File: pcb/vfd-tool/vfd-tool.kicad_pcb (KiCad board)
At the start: 4 copper layers, 95 x 50 mm, 170 parts, among them J1 Conn_ARM_SWD_TagConnect_TC203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, J2 USB_C_Receptacle_USB2.0, J3 Micro_SD_Card, J4 Conn_01x10, J5 Raspberry_Pi_2_3, J6 Conn_02x15_Odd_Even, J7 Conn_02x15_Odd_Even, J8 Conn_02x08_Odd_Even, J9 Conn_01x02_Socket, SW1 SW_Push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

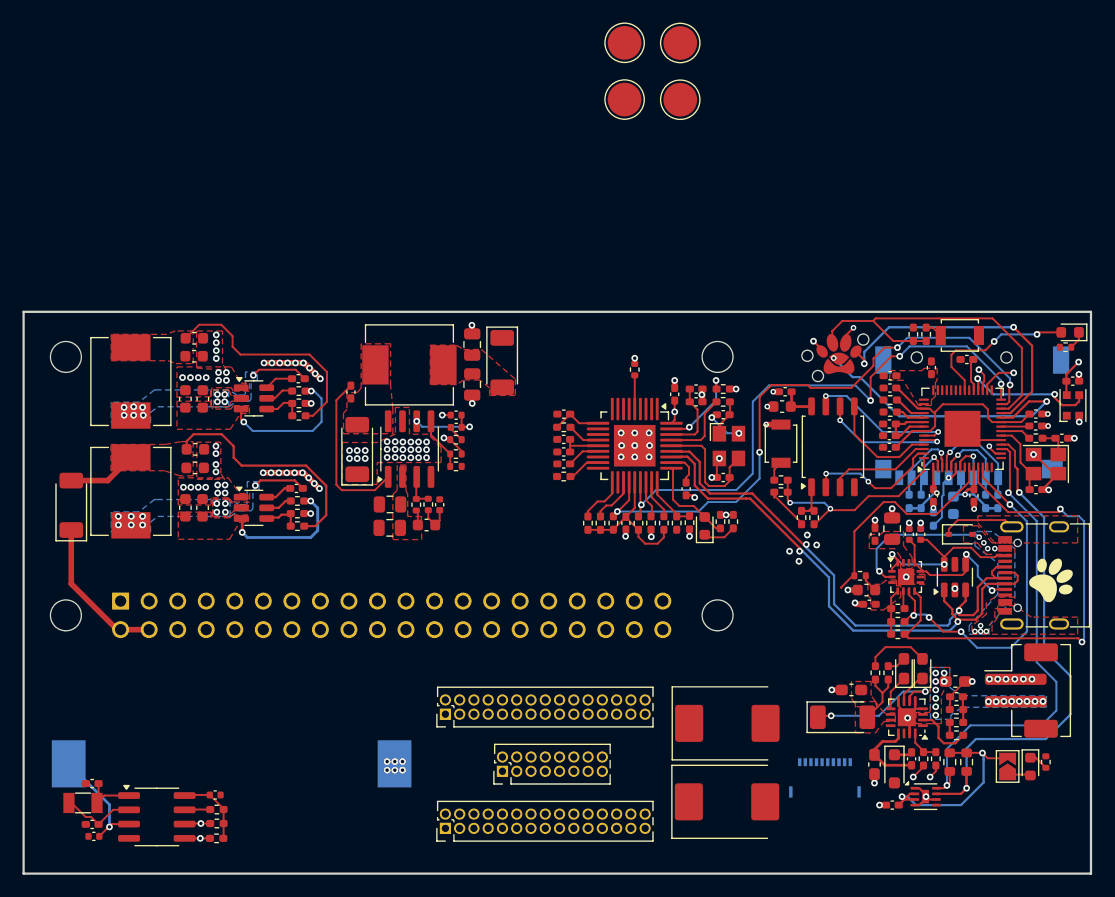
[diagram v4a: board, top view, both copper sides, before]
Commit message: finished interconnect, started on internal power layer
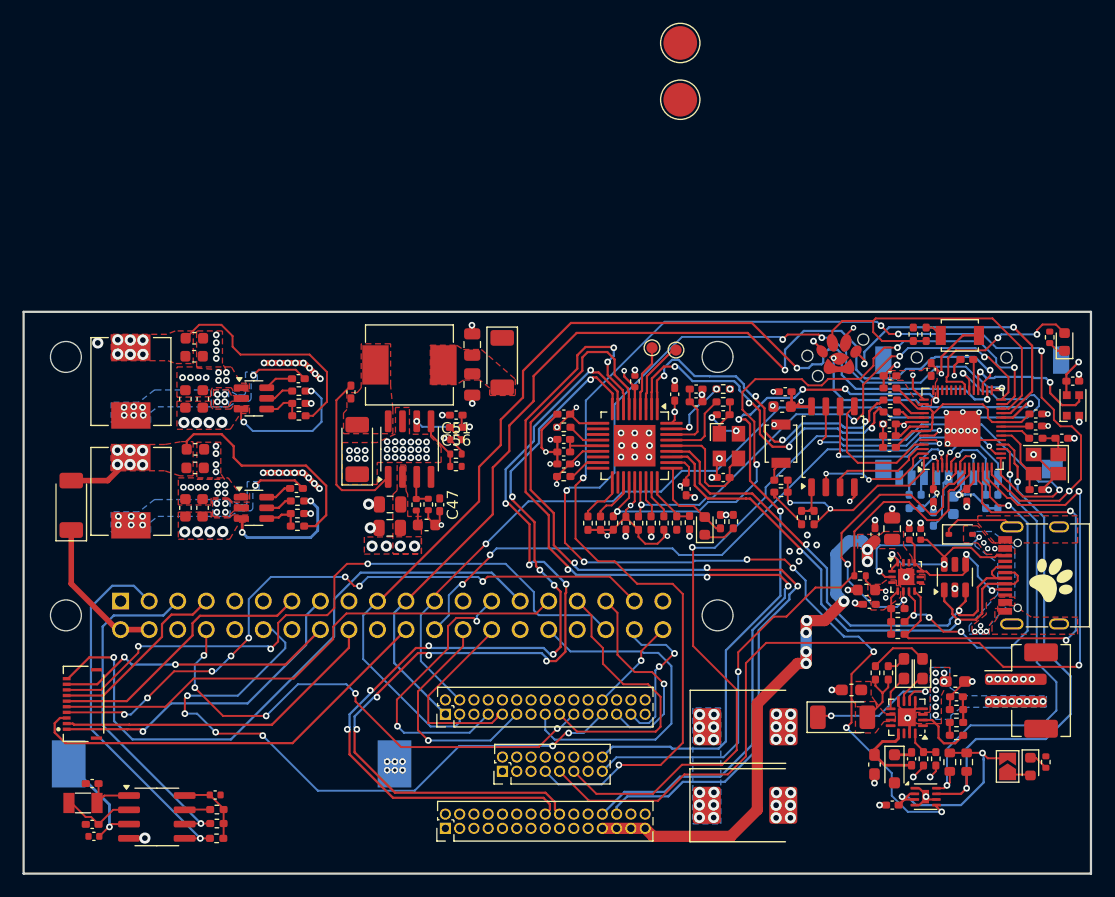
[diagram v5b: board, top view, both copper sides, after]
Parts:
- C47, C51, C56: footprint Capacitor_SMD:C_0402_1005Metric -> Capacitor_SMD:C_0402_1005Metric_Pad0.74x0.62mm_HandSolder
- J4: moved to F.Cu
- TP3, TP4: footprint TestPoint:TestPoint_Pad_D3.0mm -> TestPoint:TestPoint_Pad_D1.0mm
- moved J4 67.7 mm to (145.6, 108.3), turned to 90 degrees
- moved TP4 27.7 mm to (199.8, 76.8)
- moved TP3 22.2 mm to (197.7, 76.6)
- moved R20 1.66 mm to (233.1, 75.7), turned to 90 degrees
- moved D7 1.63 mm to (206.0, 110.3)
- moved D8 1.63 mm to (205.9, 117.3)
- moved C16 1.05 mm to (196.1, 79.6)
- moved D4 0.98 mm to (234.4, 76.1), turned to 90 degrees
- moved C21 0.64 mm to (225.7, 89.7)
- moved C24 0.15 mm to (222.5, 78.5)
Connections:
- J6 pad 11: VBUS -> 5V
- J6 pad 13: GND -> 5V
- J6 pad 15: 3V3 -> GND
- J6 pad 17: 3V3 -> VBUS
- J6 pad 19: 5V -> VBUS
- J6 pad 21: 5V -> VBUS
- J6 pad 26: EXTRA_USB4_D- -> EXTRA_USB3_D-
- J6 pad 7: VBUS -> 3V3
- J6 pad 9: VBUS -> 3V3
- J8 pad 10: GND -> unconnected-(J8-Pin_10-Pad10)
- J8 pad 12: RP2040_GPIO27 -> unconnected-(J8-Pin_12-Pad12)
- J8 pad 14: RP2040_GPIO28 -> unconnected-(J8-Pin_14-Pad14)
- U9 pad 5: GPIO16 -> BATT_INT
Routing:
- net RP2040_GPIO11: track 0.00 -> 120.2 mm, vias 0 -> 6
- net BATT_INT: track 0.20 -> 111.8 mm, vias 0 -> 10
- net MOSI_INTER: track 3.31 -> 93.2 mm, vias 1 -> 2
- net MISO_INTER: track 2.08 -> 89.5 mm, vias 1 -> 2
- net RP2040_GPIO10: track 0.00 -> 85.1 mm, vias 0 -> 2
- net RP2040_GPIO12: track 0.00 -> 84.9 mm, vias 0 -> 2
- net EXTRA_USB3_D+: track 0.00 -> 84.3 mm, vias 0 -> 5
- net EXTRA_USB4_D-: track 0.00 -> 83.5 mm, vias 0 -> 8
- net SCLK_INTER: track 0.00 -> 83.1 mm, vias 0 -> 2
- net EXTRA_USB3_D-: track 0.00 -> 82.6 mm, vias 0 -> 3
- net EXTRA_USB4_D+: track 0.00 -> 79.8 mm, vias 0 -> 8
- net RP2040_GPIO29: track 0.00 -> 64.4 mm, vias 0 -> 5
- net Net-(D7-A): track 0.00 -> 63.1 mm, vias 0 -> 6
- net GSBLK: track 0.00 -> 59.7 mm, vias 0 -> 8
- net BLK: track 0.00 -> 59.2 mm, vias 0 -> 3
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- added copper zone on In2.Cu, net 3V3
- added copper zone on B.Cu, net EXT_PWR
- added copper zone on In2.Cu, net EXT_PWR
- added copper zone on In1.Cu, net GND
- added copper zone on In2.Cu, net VSYS

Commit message: Power plane kinda done
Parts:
- moved TP2 72.4 mm to (213.7, 120.7)
- moved TP1 60.0 mm to (213.2, 113.1)
- turned D14 to 90 degrees
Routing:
- net 5V: track 43.9 -> 193.8 mm, vias 7 -> 12
- net 3V3: track 159.6 -> 213.1 mm, vias 27 -> 31
- net RPI0_GPIO17: track 0.00 -> 43.7 mm, vias 0 -> 3
- net RPI0_GPIO15: track 0.00 -> 43.7 mm, vias 0 -> 6
- net GND: track 102.9 -> 116.9 mm, vias 154 -> 157
- net Net-(D14-A): track 0.00 -> 13.5 mm, vias 0 -> 2
- net VSYS: track 37.0 -> 47.2 mm, vias 14 -> 21
- net VBUS: track 59.6 -> 69.2 mm
- net CHRG_CTRL_2: track 1.40 -> 8.01 mm
- net VCONN: track 50.8 -> 55.9 mm
- net CHRG_CTRL_1: track 1.23 -> 6.21 mm
- net Net-(U10-SS): track 0.00 -> 2.23 mm
- net EXT_PWR: track 44.7 -> 46.4 mm
- net SCLK_INTER: track 83.1 -> 84.3 mm
- net RP2040_CE: track 59.9 -> 61.0 mm
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- added copper zone on In2.Cu, net 5V
- added copper zone on In2.Cu, net VBUS

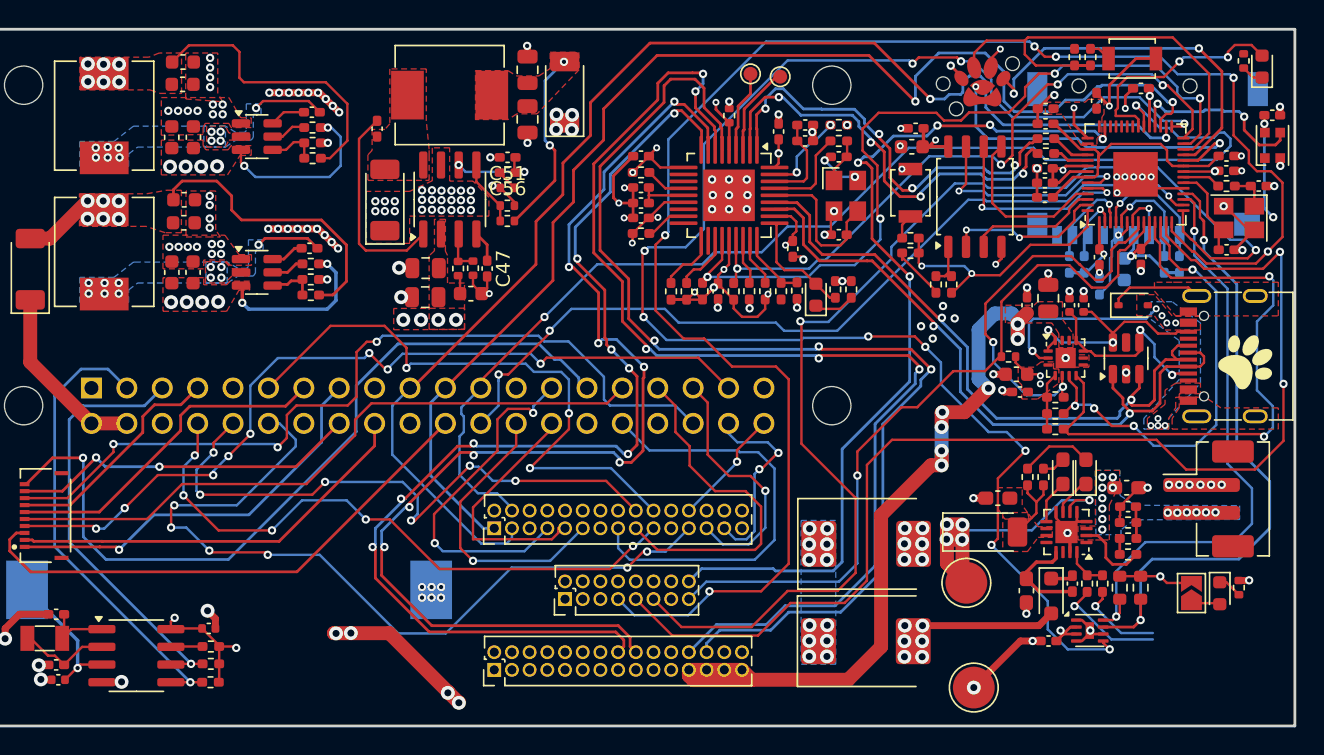
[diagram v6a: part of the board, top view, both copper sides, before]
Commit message: DRC Fixed and added solder jumpers
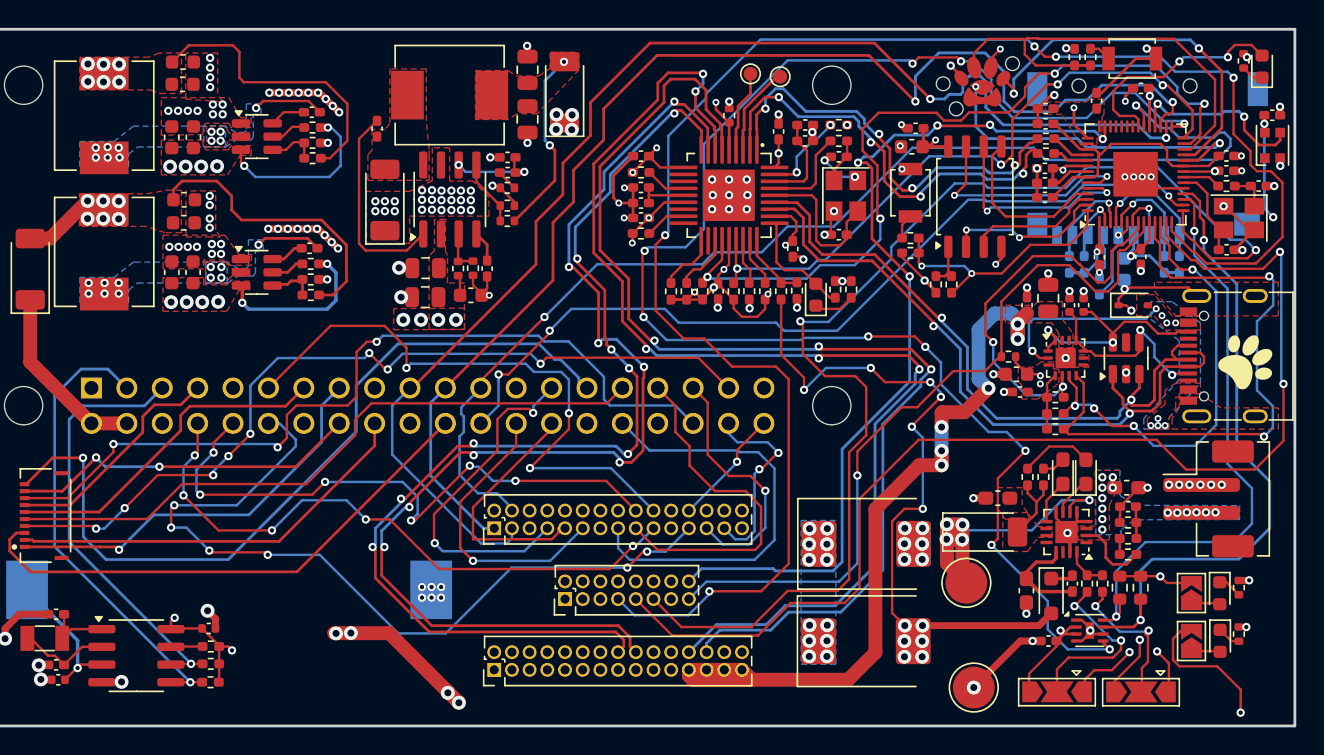
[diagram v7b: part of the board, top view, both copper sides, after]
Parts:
- added D15: LED, LED_SMD:LED_0603_1608Metric, F.Cu at (231.4, 117.3)
- added JP2: SolderJumper_2_Open, Jumper:SolderJumper-2_P1.3mm_Open_TrianglePad1.0x1.5mm, F.Cu at (229.3, 117.3)
- added JP3: SolderJumper_3_Open, Jumper:SolderJumper-3_P2.0mm_Open_TrianglePad1.0x1.5mm, F.Cu at (219.7, 121.0)
- added JP4: SolderJumper_3_Open, Jumper:SolderJumper-3_P2.0mm_Open_TrianglePad1.0x1.5mm, F.Cu at (225.7, 121.0)
- added R58: 1k, Resistor_SMD:R_0402_1005Metric, F.Cu at (232.7, 116.8)
- moved C45 0.12 mm to (177.6, 92.5)
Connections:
- J7 pad 2: RGB_DOUT -> unconnected-(J7-Pin_2-Pad2)
- U1 pad 36: CHRG_CTRL_1 -> unconnected-(U1-GPIO24-Pad36)
- U1 pad 37: CHRG_CTRL_2 -> unconnected-(U1-GPIO25-Pad37)
- U1 pad 38: BATT_MONITOR -> unconnected-(U1-GPIO26_ADC0-Pad38)
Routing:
- net VBUS: track 69.2 -> 107.5 mm, vias 15 -> 21
- net Net-(J5-3V3-Pad1): track 0.00 -> 21.7 mm
- net GND: track 116.9 -> 129.0 mm, vias 157 -> 161
- net 5V: track 193.8 -> 203.7 mm, vias 12 -> 13
- net 3V3: track 213.1 -> 221.3 mm, vias 31 -> 34
- net CHRG_CTRL_2: track 8.01 -> 13.8 mm, vias 1 -> 2
- net CHRG_CTRL_1: track 6.21 -> 10.7 mm, vias 1 -> 2
- net Net-(D15-A): track 0.00 -> 2.08 mm
- net RP2040_GPIO12: track 85.0 -> 86.9 mm
- net Net-(D15-K): track 0.00 -> 1.68 mm
- net RP2040_GPIO10: track 84.2 -> 83.1 mm
- net QSPI_SD3: track 16.3 -> 16.9 mm
- net SWD_RP2040: track 26.6 -> 27.1 mm
- net ONEWIRE_DETECT: track 53.6 -> 54.1 mm
- net VCONN: track 55.9 -> 56.3 mm, vias 7 -> 6
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
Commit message: 3D fixed + silkscreen
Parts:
- added G**: Paw-Connect_Silk_Full, Paw-Connect:Paw-Connect_Silk_Full, F.Cu at (144.6, 83.7)
- added REF**: OSHW-Logo_5.7x6mm_SilkScreen, Symbol:OSHW-Logo_5.7x6mm_SilkScreen, F.Cu at (167.1, 109.6)
- U2: footprint USB2514B_M2:36-SQFN-EXPOSED-PAD -> USB2514B-I_M2:QFN50P600X600X100-37N
- moved G** 0.81 mm to (232.9, 96.5)
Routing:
- net 3V3: track 221.3 -> 224.3 mm
- net 5V: track 203.7 -> 206.3 mm, vias 13 -> 14
- net BATT_INT: track 112.1 -> 109.7 mm
- net HUB_SUSP: track 8.13 -> 8.78 mm
- net RP2040_D-: track 30.9 -> 31.4 mm
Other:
- board text added: "+"
- board text added: "-"
- board text added: "0 0 = 0.1A 0 1 = 0.5A 1 1 = SUSP"
- board text added: "3V3"
- board text added: "5V"
- board text added: "Approved by Flopsy"
- board text added: "Battery"
- board text added: "Boot"
- board text added: "CHG"
- board text added: "D+"
- board text added: "D-"
- board text added: "GND"
- board text added: "Geenk Engineering"
- board text added: "HV step down (20V)"
- board text added: "Hoid was here"
- board text added: "Honk!"
- board text added: "JLCJLCJLCJLC"
- board text added: "MCU"
- board text added: "MCU Carrier"
- board text added: "PCB3D_BR_MCU"
- board text added: "PCB3D_TL_MCU"
- board text added: "PG"
- board text added: "RTC"
- board text added: "Rst"
- board text added: "SUSP"
- board text added: "SWD"
- board text added: "To VFD"
- board text added: "USB"
- board text added: "USB hub"
- board text added: "V0.1A"
- board text added: "VSYS"
